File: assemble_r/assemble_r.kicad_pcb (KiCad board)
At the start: 2 copper layers, 128.5 x 102.6 mm, 51 parts, among them SW23 SW_Push, SW24 SW_Push, SW25 SW_Push, SW26 SW_Push, SW27 SW_Push, SW28 SW_Push, SW29 SW_Push, SW30 SW_Push, SW31 SW_Push, SW32 SW_Push, SW33 SW_Push, SW34 SW_Push, SW35 SW_Push, SW36 SW_Push, SW37 SW_Push, SW38 SW_Push, SW39 SW_Push, SW40 SW_Push, SW41 SW_Push, SW42 SW_Push, SW43 SW_Push, SW44 SW_Push, SW45 SW_SPDT, U23 Micon_BLEMicroPro

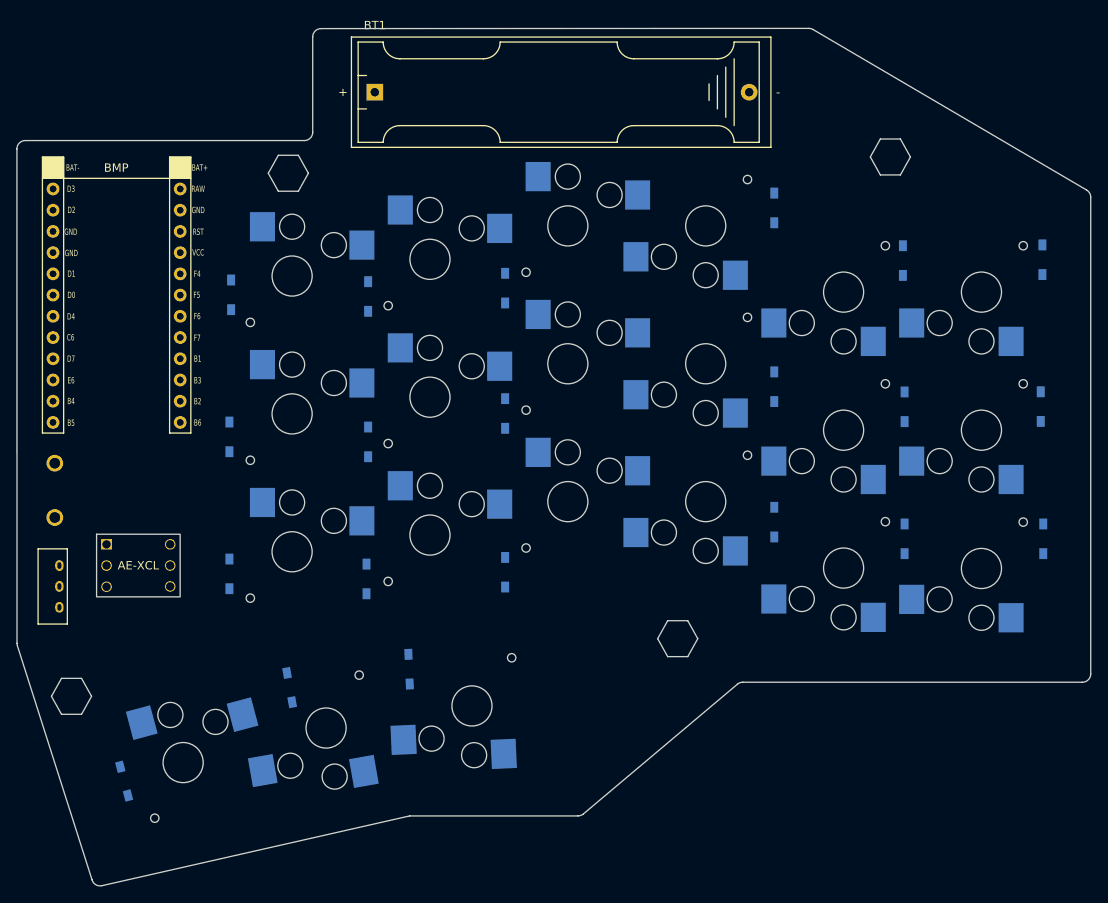
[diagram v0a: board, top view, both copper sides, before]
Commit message: feat: wiring right hand
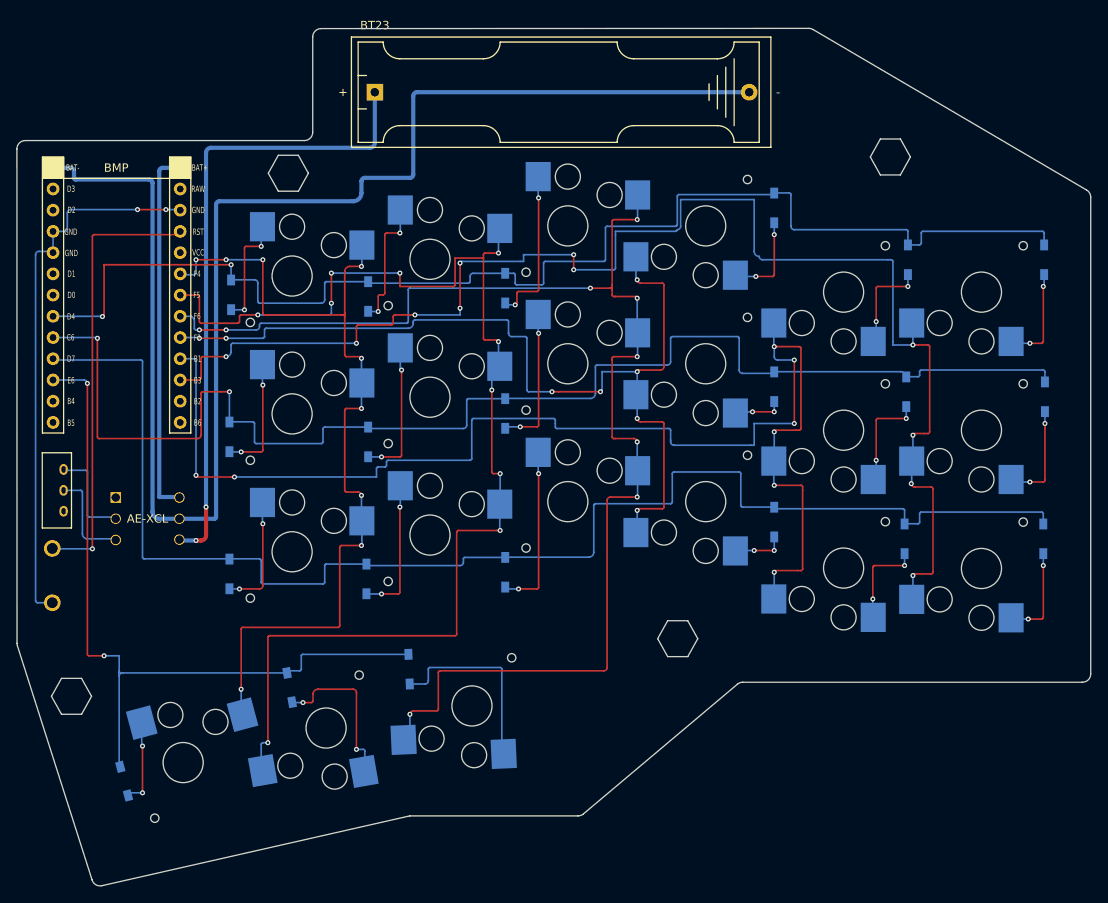
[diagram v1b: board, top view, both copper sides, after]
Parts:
- removed BT1: Battery_Cell, kbd_Parts:Battery_AAA
- added BT23: Battery_Cell, kbd_Parts:Battery_AAA, F.Cu at (86.8, 55.4)
- SW44: value SW_Push -> SW_SPDT; footprint kbd_Parts:ResetSW -> kbd_Parts:TGSW_MSK-12D19
- SW45: value SW_SPDT -> SW_Push; footprint kbd_Parts:TGSW_MSK-12D19 -> kbd_Parts:ResetSW
- moved AE-XCL 5.71 mm to (59.6, 106.4)
- moved D39 1.81 mm to (150.4, 91.2)
- moved SW45 1.32 mm to (48.2, 113.2)
- moved D42 1.28 mm to (167.0, 91.8)
- moved D38 0.61 mm to (150.6, 75.4)
- moved D41 0.20 mm to (166.9, 75.4)
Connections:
- AE-XCL pad 2: Net-(AE-XCL102D333CR-G1-EN) -> Net-(AE-XCL102D333CR-G23-EN)
- AE-XCL pad 3: Net-(SW45-B) -> Net-(SW44-B)
- D38 pad 1: Row2 -> Row0
- D39 pad 1: Row0 -> Row1
- D40 pad 1: Row1 -> Row2
- D41 pad 1: Row2 -> Row0
- D42 pad 1: Row0 -> Row1
- D43 pad 1: Row1 -> Row2
- SW38 pad 1: Col5 -> Col4
- SW41 pad 1: Col4 -> Col5
- SW44 pad 1: Reset -> unconnected-(SW44-A-Pad1)
- SW44 pad 2: GND -> Net-(SW44-B)
- SW45 pad 1: unconnected-(SW45-A-Pad1) -> Reset
- SW45 pad 2: Net-(SW45-B) -> GND
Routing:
- net Bat-: track 0.00 -> 174.2 mm
- net Col5: track 0.00 -> 170.1 mm, vias 0 -> 11
- net Row2: track 0.00 -> 165.9 mm
- net Col2: track 0.00 -> 161.7 mm, vias 0 -> 9
- net Row1: track 0.00 -> 160.5 mm, vias 0 -> 2
- net Col4: track 0.00 -> 156.6 mm, vias 0 -> 8
- net Row0: track 0.00 -> 152.7 mm, vias 0 -> 2
- net Col1: track 0.00 -> 148.2 mm, vias 0 -> 10
- net Col3: track 0.00 -> 111.9 mm, vias 0 -> 8
- net Col0: track 0.00 -> 106.1 mm, vias 0 -> 9
- net Row3: track 0.00 -> 91.5 mm, vias 0 -> 2
- net Net-(BT23-+): track 0.00 -> 76.1 mm, vias 0 -> 2
- net GND: track 0.00 -> 65.9 mm, vias 0 -> 2
- net Reset: track 0.00 -> 52.4 mm, vias 0 -> 1
- net Bat+: track 0.00 -> 44.1 mm
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
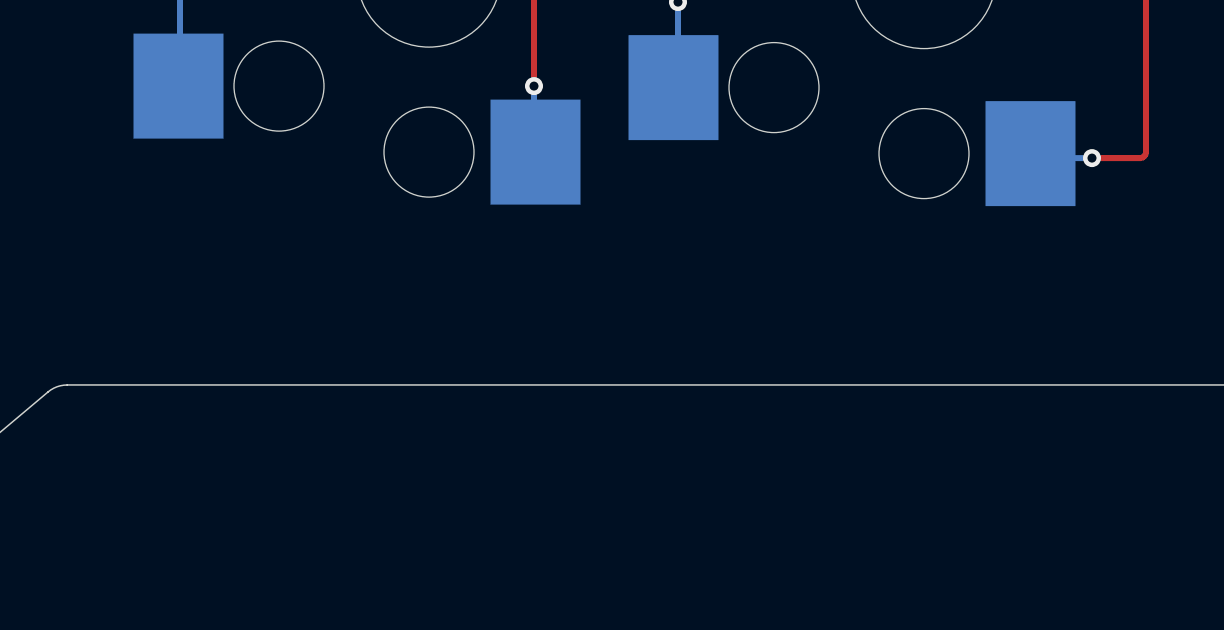
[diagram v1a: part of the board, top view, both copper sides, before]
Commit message: feat: add signature and version
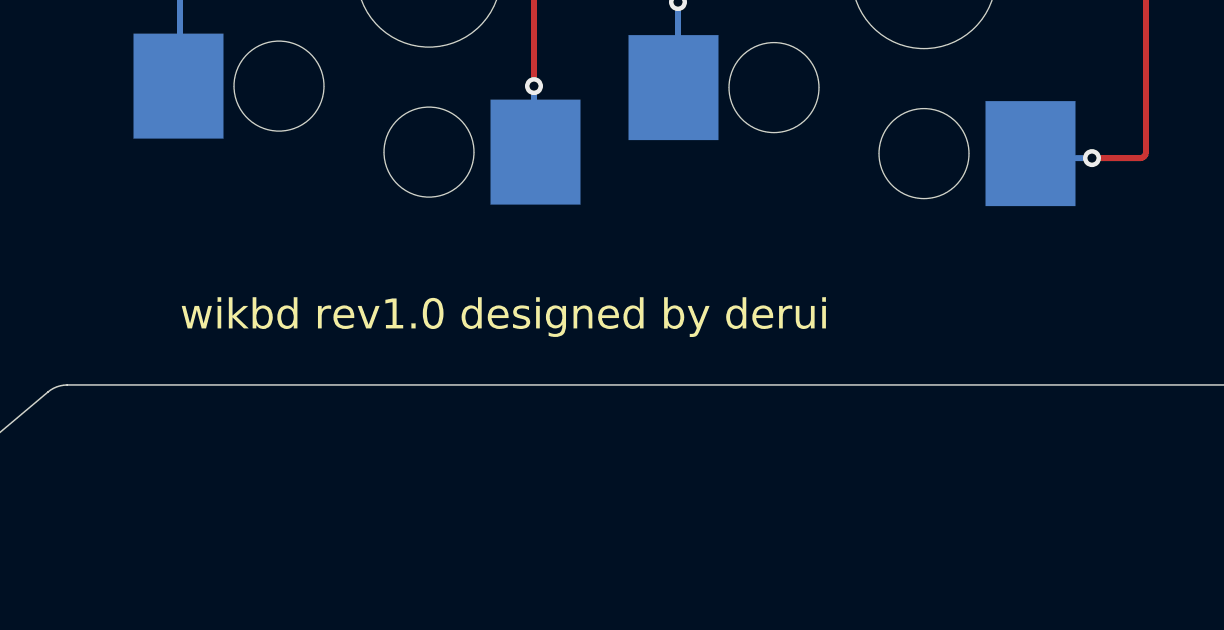
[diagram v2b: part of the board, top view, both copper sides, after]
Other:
- board text added: "wikbd rev1.0 designed by derui"
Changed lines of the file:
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@@
 		(fp_line
 			(start 0.5 8.2)
-			(end 0.5 3.599999)
+			(end 0.5 3.599998)
 			(stroke
 				(width 0.15)
@@
 		(fp_line
 			(start -7.305 2.375)
-			(end -7.304999 5.025)
+			(end -7.304998 5.025)
 			(stroke
 				(width 0.15)
@@
 		(fp_arc
 			(start -1.275 3.575)
-			(mid -2.10585 3.230851)
+			(mid -2.10585 3.230852)
 			(end -2.450001 2.4)
 			(stroke
@@
 			(start -6.305 6.025)
 			(mid -7.012107 5.732107)
-			(end -7.304999 5.025)
+			(end -7.304998 5.025)
 			(stroke
 				(width 0.15)
@@
 		)
 		(pad "" np_thru_hole circle
-			(at 5 -5.550001 195)
+			(at 5 -5.550002 195)
 			(size 1 1)
 			(drill oval 1)
@@
 		)
 		(fp_line
-			(start -0.850001 8.2)
+			(start -0.850003 8.2)
 			(end -0.85 3.6)
 			(stroke
@@
 		(fp_line
 			(start 0.65 8.2)
-			(end 0.649999 3.6)
+			(end 0.649998 3.6)
 			(stroke
 				(width 0.15)
@@
 		)
 		(fp_arc
-			(start -6.305 6.024999)
+			(start -6.305 6.024998)
 			(mid -7.012107 5.732107)
 			(end -7.305 5.025)
@@
 		)
 		(fp_line
-			(start -4.6 6.000001)
+			(start -4.6 6.000003)
 			(end -4.6 1.4)
 			(stroke
@@
 		)
 		(fp_line
-			(start -1.3 7.989999)
+			(start -1.3 7.989997)
 			(end -1.3 3.6)
 			(stroke
@@
 		(fp_line
 			(start -0.4 8.2)
-			(end -0.399999 3.6)
+			(end -0.399997 3.6)
 			(stroke
 				(width 0.15)
@@
 		)
 		(fp_line
-			(start 1.85 7.660001)
+			(start 1.85 7.660002)
 			(end 1.85 4.13)
 			(stroke
@@
 		)
 		(pad "" np_thru_hole circle
-			(at 5.000001 -5.55 2.5)
+			(at 5.000003 -5.55 2.5)
 			(size 1 1)
 			(drill oval 1)
@@
 		(layer "Edge.Cuts")
 	)
+	(gr_text "wikbd rev1.0 designed by derui"
+		(at 134.6 124.2 0)
+		(layer "F.SilkS")
+		(effects
+			(font
+				(size 1 1)
+				(thickness 0.1)
+			)
+			(justify left bottom)
+		)
+	)
 	(segment

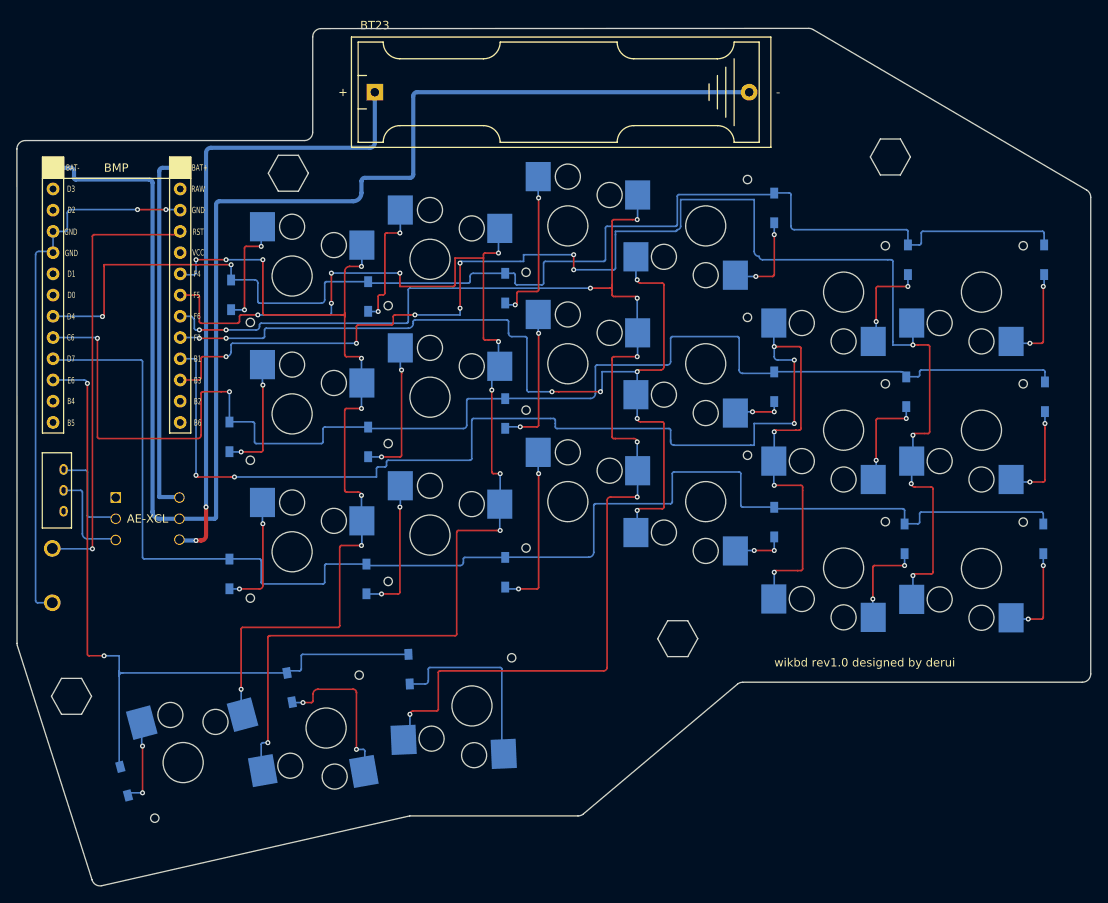
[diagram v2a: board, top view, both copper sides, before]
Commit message: feat: change PCB outline
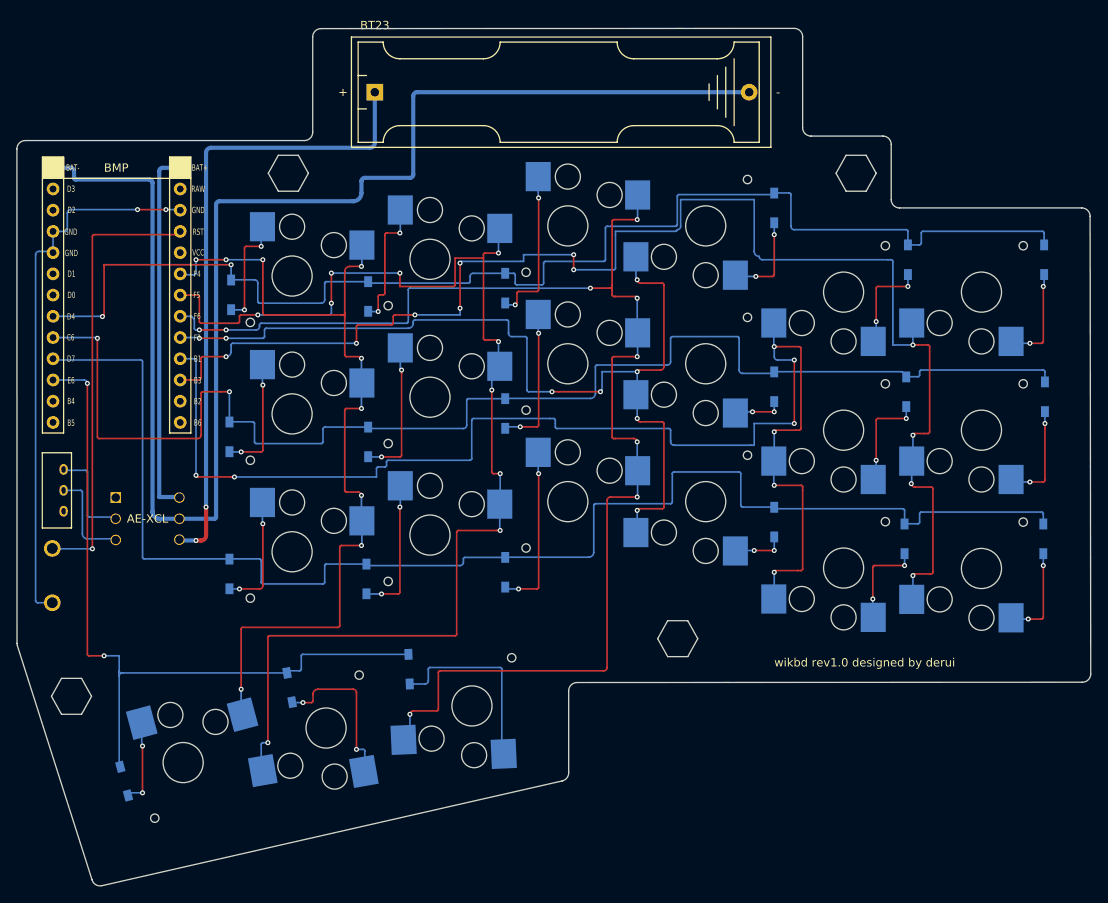
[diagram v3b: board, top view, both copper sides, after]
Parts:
- moved Ref** 4.54 mm to (144.4, 65.0)
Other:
- outline, holes or cut-outs redrawn
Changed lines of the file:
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@@
 	(footprint "kbd_Hole:m2_Spacer_Hole_hex"
 		(layer "F.Cu")
-		(at 148.5 63.1)
+		(at 144.4 65.05)
 		(descr "Mounting Hole 2.2mm, no annular, M2")
 		(tags "mounting hole 2.2mm no annular m2")
@@
 		)
 		(fp_line
-			(start -4.6 6.000003)
+			(start -4.6 6.000004)
 			(end -4.6 1.4)
 			(stroke
@@
 		)
 		(fp_line
-			(start -1.3 7.989997)
+			(start -1.3 7.989996)
 			(end -1.3 3.6)
 			(stroke
@@
 		(fp_line
 			(start -0.4 8.2)
-			(end -0.399997 3.6)
+			(end -0.399996 3.6)
 			(stroke
 				(width 0.15)
@@
 		)
 		(pad "" np_thru_hole circle
-			(at 5.000003 -5.55 2.5)
+			(at 5.000004 -5.55 2.5)
 			(size 1 1)
 			(drill oval 1)
@@
 		(layer "Edge.Cuts")
 	)
-	(gr_line
-		(start 80.36523 47.737079)
-		(end 138.743943 47.712506)
+	(gr_arc
+		(start 149.6 69.2)
+		(mid 148.892893 68.907107)
+		(end 148.6 68.2)
 		(stroke
 			(width 0.05)
@@
 	)
 	(gr_line
-		(start 130.198983 126.197589)
-		(end 111.757319 141.727411)
+		(start 80.36523 47.737079)
+		(end 136.999574 47.712933)
 		(stroke
 			(width 0.05)
@@
 		(layer "Edge.Cuts")
 	)
-	(gr_line
-		(start 139.25 47.85)
-		(end 171.984208 67.056232)
+	(gr_arc
+		(start 110 126.999389)
+		(mid 110.292681 126.292505)
+		(end 110.999389 125.99939)
 		(stroke
 			(width 0.05)
@@
 	)
 	(gr_line
-		(start 54.139956 150.312491)
-		(end 90.978151 141.9625)
+		(start 139 60.6)
+		(end 147.6 60.6)
 		(stroke
 			(width 0.05)
@@
 		(layer "Edge.Cuts")
 	)
-	(gr_arc
-		(start 79.365651 60.1375)
-		(mid 79.072755 60.844589)
-		(end 78.365651 61.1375)
+	(gr_line
+		(start 54.139956 150.312491)
+		(end 109.221904 137.777077)
 		(stroke
 			(width 0.05)
@@
 		(layer "Edge.Cuts")
 	)
-	(gr_arc
-		(start 138.743943 47.7125)
-		(mid 139.006145 47.747489)
-		(end 139.25 47.85)
+	(gr_line
+		(start 110 136.802009)
+		(end 110 126.999389)
 		(stroke
 			(width 0.05)
@@
 		(layer "Edge.Cuts")
 	)
-	(gr_line
-		(start 90.978151 141.9625)
-		(end 111.113183 141.9625)
+	(gr_arc
+		(start 79.365651 60.1375)
+		(mid 79.072755 60.844589)
+		(end 78.365651 61.1375)
 		(stroke
 			(width 0.05)
@@
 		(layer "Edge.Cuts")
 	)
-	(gr_arc
-		(start 111.757319 141.727411)
-		(mid 111.456027 141.901882)
-		(end 111.113183 141.9625)
+	(gr_line
+		(start 172.4014 70.198599)
+		(end 172.478151 124.9625)
 		(stroke
 			(width 0.05)
@@
 		(layer "Edge.Cuts")
 	)
-	(gr_arc
-		(start 130.198983 126.197589)
-		(mid 130.500275 126.023119)
-		(end 130.843119 125.9625)
+	(gr_line
+		(start 148.6 61.6)
+		(end 148.6 68.2)
 		(stroke
 			(width 0.05)
@@
 	)
 	(gr_arc
+		(start 139 60.6)
+		(mid 138.292893 60.307107)
+		(end 138 59.6)
+		(stroke
+			(width 0.05)
+			(type default)
+		)
+		(layer "Edge.Cuts")
+	)
+	(gr_arc
 		(start 44.025412 121.610664)
 		(mid 43.990032 121.46065)
@@
 	)
 	(gr_line
-		(start 171.478151 125.9625)
-		(end 130.843119 125.9625)
+		(start 138 48.712932)
+		(end 138 59.6)
+		(stroke
+			(width 0.05)
+			(type default)
+		)
+		(layer "Edge.Cuts")
+	)
+	(gr_arc
+		(start 110 136.802009)
+		(mid 109.781631 137.425741)
+		(end 109.221904 137.777077)
 		(stroke
 			(width 0.05)
@@
 	)
 	(gr_arc
-		(start 171.984208 67.056232)
-		(mid 172.345937 67.421762)
-		(end 172.478151 67.918732)
+		(start 136.999574 47.712933)
+		(mid 137.706956 48.005675)
+		(end 138 48.712932)
 		(stroke
 			(width 0.05)
@@
 	)
 	(gr_line
-		(start 172.478151 67.918732)
-		(end 172.478151 124.9625)
+		(start 149.6 69.2)
+		(end 171.401401 69.2)
 		(stroke
 			(width 0.05)
@@
 		(stroke
 			(width 0.05)
+			(type default)
+		)
+		(layer "Edge.Cuts")
+	)
+	(gr_arc
+		(start 147.6 60.6)
+		(mid 148.307107 60.892893)
+		(end 148.6 61.6)
+		(stroke
+			(width 0.05)
+			(type default)
+		)
+		(layer "Edge.Cuts")
+	)
+	(gr_arc
+		(start 171.401401 69.2)
+		(mid 172.108012 69.492398)
+		(end 172.4014 70.198599)
+		(stroke
+			(width 0.05)
+			(type default)
+		)
+		(layer "Edge.Cuts")
+	)
+	(gr_line
+		(start 110.999389 125.99939)
+		(end 171.478151 125.96245)
+		(stroke
+			(width 0.05)
